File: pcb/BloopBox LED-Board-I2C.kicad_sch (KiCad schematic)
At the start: 14 parts, among them J1 I2C, J2 V_BM, U1 IS31FL3199

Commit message: fix: add part numbers
Add missing LSCS Part numbers
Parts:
- removed C2: 1u, Capacitor_SMD:C_0402_1005Metric, symbol Device:C_Small
- removed C3: 100n, Capacitor_SMD:C_0402_1005Metric, symbol Device:C_Small
- C1: LCSC (none) -> C52923
- C4, C5: LCSC (none) -> C1525
- R1: LCSC (none) -> C25741
- U1: footprint Package_DFN_QFN:QFN-20-1EP_3x3mm_P0.4mm_EP1.65x1.65mm -> Package_DFN_QFN:QFN-20-1EP_3x3mm_P0.4mm_EP1.65x1.65mm_ThermalVias
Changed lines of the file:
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@@
   (junction (at 45.72 127) (diameter 0) (color 0 0 0 0)
   )
-  (junction (at 104.14 73.66) (diameter 0) (color 0 0 0 0)
-  )
   (junction (at 71.12 127) (diameter 0) (color 0 0 0 0)
   )
   (junction (at 71.12 81.28) (diameter 0) (color 0 0 0 0)
-  )
-  (junction (at 96.52 73.66) (diameter 0) (color 0 0 0 0)
   )
   (junction (at 121.92 73.66) (diameter 0) (color 0 0 0 0)
@@
     (stroke (width 0) (type default) (color 0 0 0 0))
   )
-  (wire (pts (xy 71.12 73.66) (xy 96.52 73.66))
-    (stroke (width 0) (type default) (color 0 0 0 0))
-  )
   (wire (pts (xy 177.8 78.74) (xy 177.8 73.66))
     (stroke (width 0) (type default) (color 0 0 0 0))
@@
     (stroke (width 0) (type default) (color 0 0 0 0))
   )
-  (wire (pts (xy 104.14 81.28) (xy 104.14 83.82))
-    (stroke (width 0) (type default) (color 0 0 0 0))
-  )
   (wire (pts (xy 83.82 115.57) (xy 182.88 115.57))
     (stroke (width 0) (type default) (color 0 0 0 0))
@@
     (stroke (width 0) (type default) (color 0 0 0 0))
   )
-  (wire (pts (xy 96.52 73.66) (xy 96.52 76.2))
-    (stroke (width 0) (type default) (color 0 0 0 0))
-  )
   (wire (pts (xy 68.58 81.28) (xy 71.12 81.28))
     (stroke (width 0) (type default) (color 0 0 0 0))
@@
     (stroke (width 0) (type default) (color 0 0 0 0))
   )
-  (wire (pts (xy 104.14 73.66) (xy 121.92 73.66))
-    (stroke (width 0) (type default) (color 0 0 0 0))
-  )
   (wire (pts (xy 149.86 73.66) (xy 121.92 73.66))
     (stroke (width 0) (type default) (color 0 0 0 0))
@@
     (stroke (width 0) (type default) (color 0 0 0 0))
   )
-  (wire (pts (xy 96.52 81.28) (xy 96.52 83.82))
-    (stroke (width 0) (type default) (color 0 0 0 0))
-  )
   (wire (pts (xy 116.84 92.71) (xy 116.84 88.9))
     (stroke (width 0) (type default) (color 0 0 0 0))
@@
     (stroke (width 0) (type default) (color 0 0 0 0))
   )
-  (wire (pts (xy 96.52 73.66) (xy 104.14 73.66))
+  (wire (pts (xy 71.12 73.66) (xy 121.92 73.66))
     (stroke (width 0) (type default) (color 0 0 0 0))
   )
@@
   )
   (wire (pts (xy 53.34 110.49) (xy 53.34 127))
-    (stroke (width 0) (type default) (color 0 0 0 0))
-  )
-  (wire (pts (xy 104.14 73.66) (xy 104.14 76.2))
     (stroke (width 0) (type default) (color 0 0 0 0))
   )
@@
       (effects (font (size 1.27 1.27)) hide)
     )
+    (property "LCSC" "C25741" (id 4) (at 36.83 113.03 0)
+      (effects (font (size 1.27 1.27)) hide)
+    )
     (pin "1")
     (pin "2")
@@
     )
     (pin "1")
-  )
-  (symbol (lib_id "Device:C_Small") (at 96.52 78.74 180) (unit 1)
-    (in_bom yes) (on_board yes) (fields_autoplaced)
-    (property "Reference" "C2" (id 0) (at 98.8441 77.8989 0)
-      (effects (font (size 1.27 1.27)) (justify right))
-    )
-    (property "Value" "1u" (id 1) (at 98.8441 80.4358 0)
-      (effects (font (size 1.27 1.27)) (justify right))
-    )
-    (property "Footprint" "Capacitor_SMD:C_0402_1005Metric" (id 2) (at 96.52 78.74 0)
-      (effects (font (size 1.27 1.27)) hide)
-    )
-    (property "Datasheet" "~" (id 3) (at 96.52 78.74 0)
-      (effects (font (size 1.27 1.27)) hide)
-    )
-    (pin "1")
-    (pin "2")
   )
   (symbol (lib_id "power:GND") (at 60.96 81.28 270) (unit 1)
@@
       (effects (font (size 1.27 1.27)) (justify left))
     )
-    (property "Footprint" "Package_DFN_QFN:QFN-20-1EP_3x3mm_P0.4mm_EP1.65x1.65mm" (id 2) (at 71.12 82.55 0)
+    (property "Footprint" "Package_DFN_QFN:QFN-20-1EP_3x3mm_P0.4mm_EP1.65x1.65mm_ThermalVias" (id 2) (at 71.12 82.55 0)
       (effects (font (size 1.27 1.27)) hide)
     )
@@
     (pin "9")
   )
-  (symbol (lib_id "power:GND") (at 104.14 83.82 0) (unit 1)
-    (in_bom yes) (on_board yes) (fields_autoplaced)
-    (property "Reference" "#PWR07" (id 0) (at 104.14 90.17 0)
-      (effects (font (size 1.27 1.27)) hide)
-    )
-    (property "Value" "GND" (id 1) (at 106.045 85.5238 0)
-      (effects (font (size 1.27 1.27)) (justify left))
-    )
-    (property "Footprint" "" (id 2) (at 104.14 83.82 0)
-      (effects (font (size 1.27 1.27)) hide)
-    )
-    (property "Datasheet" "" (id 3) (at 104.14 83.82 0)
-      (effects (font (size 1.27 1.27)) hide)
-    )
-    (pin "1")
-  )
   (symbol (lib_id "Connector_Generic:Conn_01x01") (at 30.48 53.34 180) (unit 1)
     (in_bom yes) (on_board yes) (fields_autoplaced)
@@
       (effects (font (size 1.27 1.27)) hide)
     )
+    (property "LCSC" "C52923" (id 4) (at 66.04 73.66 0)
+      (effects (font (size 1.27 1.27)) hide)
+    )
     (pin "1")
     (pin "2")
@@
       (effects (font (size 1.27 1.27)) hide)
     )
-    (pin "1")
-    (pin "2")
-  )
-  (symbol (lib_id "power:GND") (at 96.52 83.82 0) (unit 1)
-    (in_bom yes) (on_board yes) (fields_autoplaced)
-    (property "Reference" "#PWR06" (id 0) (at 96.52 90.17 0)
-      (effects (font (size 1.27 1.27)) hide)
-    )
-    (property "Value" "GND" (id 1) (at 98.425 85.5238 0)
-      (effects (font (size 1.27 1.27)) (justify left))
-    )
-    (property "Footprint" "" (id 2) (at 96.52 83.82 0)
-      (effects (font (size 1.27 1.27)) hide)
-    )
-    (property "Datasheet" "" (id 3) (at 96.52 83.82 0)
-      (effects (font (size 1.27 1.27)) hide)
-    )
-    (pin "1")
+    (property "LCSC" "C1525" (id 4) (at 66.04 81.28 0)
+      (effects (font (size 1.27 1.27)) hide)
+    )
+    (pin "1")
+    (pin "2")
   )
   (symbol (lib_id "Device:C_Small") (at 45.72 113.03 180) (unit 1)
@@
       (effects (font (size 1.27 1.27)) hide)
     )
-    (pin "1")
-    (pin "2")
-  )
-  (symbol (lib_id "Device:C_Small") (at 104.14 78.74 180) (unit 1)
-    (in_bom yes) (on_board yes) (fields_autoplaced)
-    (property "Reference" "C3" (id 0) (at 106.4641 77.8989 0)
-      (effects (font (size 1.27 1.27)) (justify right))
-    )
-    (property "Value" "100n" (id 1) (at 106.4641 80.4358 0)
-      (effects (font (size 1.27 1.27)) (justify right))
-    )
-    (property "Footprint" "Capacitor_SMD:C_0402_1005Metric" (id 2) (at 104.14 78.74 0)
-      (effects (font (size 1.27 1.27)) hide)
-    )
-    (property "Datasheet" "~" (id 3) (at 104.14 78.74 0)
+    (property "LCSC" "C1525" (id 4) (at 45.72 113.03 0)
       (effects (font (size 1.27 1.27)) hide)
     )
@@
       (reference "#PWR05") (unit 1) (value "GND") (footprint "")
     )
-    (path "/dbcecde5-1d68-41ea-8940-39f26b5eec6b"
-      (reference "#PWR06") (unit 1) (value "GND") (footprint "")
-    )
-    (path "/56eb8215-4817-443a-ae37-57edd7e00e9a"
-      (reference "#PWR07") (unit 1) (value "GND") (footprint "")
-    )
     (path "/0ad71f82-5b4f-4881-8640-a72fd7d96db2"
       (reference "#PWR08") (unit 1) (value "VCC") (footprint "")
@@
       (reference "C1") (unit 1) (value "1u") (footprint "Capacitor_SMD:C_0402_1005Metric")
     )
-    (path "/200cf5e6-e58a-40f9-b45f-b55c95de0d8b"
-      (reference "C2") (unit 1) (value "1u") (footprint "Capacitor_SMD:C_0402_1005Metric")
-    )
-    (path "/e057b853-9a40-4a3e-8bf4-4b4fa06f5df1"
-      (reference "C3") (unit 1) (value "100n") (footprint "Capacitor_SMD:C_0402_1005Metric")
-    )
     (path "/cdfd3c02-6223-4acd-8411-8f5e2a574677"
       (reference "C4") (unit 1) (value "100n") (footprint "Capacitor_SMD:C_0402_1005Metric")
@@
     )
     (path "/4e91f506-e77b-4b90-ab1f-968dcca557ce"
-      (reference "U1") (unit 1) (value "IS31FL3199") (footprint "Package_DFN_QFN:QFN-20-1EP_3x3mm_P0.4mm_EP1.65x1.65mm")
-    )
-  )
+      (reference "U1") (unit 1) (value "IS31FL3199") (footprint "Package_DFN_QFN:QFN-20-1EP_3x3mm_P0.4mm_EP1.65x1.65mm_ThermalVias")
+    )
+  )

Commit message: fix: add power flags
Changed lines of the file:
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@@
     (pin "4")
+  )
+  (symbol (lib_id "power:PWR_FLAG") (at -58.42 177.8 0) (unit 1)
+    (in_bom yes) (on_board yes) (fields_autoplaced)
+    (property "Reference" "#FLG0102" (id 0) (at -58.42 175.895 0)
+      (effects (font (size 1.27 1.27)) hide)
+    )
+    (property "Value" "PWR_FLAG" (id 1) (at -58.42 174.2242 0))
+    (property "Footprint" "" (id 2) (at -58.42 177.8 0)
+      (effects (font (size 1.27 1.27)) hide)
+    )
+    (property "Datasheet" "~" (id 3) (at -58.42 177.8 0)
+      (effects (font (size 1.27 1.27)) hide)
+    )
+    (pin "1")
   )
   (symbol (lib_id "power:GND") (at 71.12 129.54 0) (unit 1)
@@
     (pin "1")
   )
+  (symbol (lib_id "power:PWR_FLAG") (at -48.26 177.8 0) (unit 1)
+    (in_bom yes) (on_board yes) (fields_autoplaced)
+    (property "Reference" "#FLG0101" (id 0) (at -48.26 175.895 0)
+      (effects (font (size 1.27 1.27)) hide)
+    )
+    (property "Value" "PWR_FLAG" (id 1) (at -48.26 174.2242 0))
+    (property "Footprint" "" (id 2) (at -48.26 177.8 0)
+      (effects (font (size 1.27 1.27)) hide)
+    )
+    (property "Datasheet" "~" (id 3) (at -48.26 177.8 0)
+      (effects (font (size 1.27 1.27)) hide)
+    )
+    (pin "1")
+  )
   (symbol (lib_id "Mechanical:MountingHole") (at 172.72 144.78 0) (unit 1)
     (in_bom yes) (on_board yes) (fields_autoplaced)
@@
     )
     (property "Datasheet" "" (id 3) (at 71.12 71.12 0)
+      (effects (font (size 1.27 1.27)) hide)
+    )
+    (pin "1")
+  )
+  (symbol (lib_id "power:VCC") (at -58.42 177.8 180) (unit 1)
+    (in_bom yes) (on_board yes) (fields_autoplaced)
+    (property "Reference" "#PWR0102" (id 0) (at -58.42 173.99 0)
+      (effects (font (size 1.27 1.27)) hide)
+    )
+    (property "Value" "VCC" (id 1) (at -57.023 179.5038 0)
+      (effects (font (size 1.27 1.27)) (justify right))
+    )
+    (property "Footprint" "" (id 2) (at -58.42 177.8 0)
+      (effects (font (size 1.27 1.27)) hide)
+    )
+    (property "Datasheet" "" (id 3) (at -58.42 177.8 0)
       (effects (font (size 1.27 1.27)) hide)
     )
@@
     (pin "4")
   )
+  (symbol (lib_id "power:GND") (at -48.26 177.8 0) (unit 1)
+    (in_bom yes) (on_board yes) (fields_autoplaced)
+    (property "Reference" "#PWR0101" (id 0) (at -48.26 184.15 0)
+      (effects (font (size 1.27 1.27)) hide)
+    )
+    (property "Value" "GND" (id 1) (at -46.355 179.5038 0)
+      (effects (font (size 1.27 1.27)) (justify left))
+    )
+    (property "Footprint" "" (id 2) (at -48.26 177.8 0)
+      (effects (font (size 1.27 1.27)) hide)
+    )
+    (property "Datasheet" "" (id 3) (at -48.26 177.8 0)
+      (effects (font (size 1.27 1.27)) hide)
+    )
+    (pin "1")
+  )
   (symbol (lib_id "Mechanical:MountingHole") (at 172.72 149.86 0) (unit 1)
     (in_bom yes) (on_board yes) (fields_autoplaced)
@@
   )
   (symbol_instances
+    (path "/7ffca218-bf34-42a3-b54e-1156e20a2407"
+      (reference "#FLG0101") (unit 1) (value "PWR_FLAG") (footprint "")
+    )
+    (path "/2f3794e2-0388-474a-a5f8-8719700774e0"
+      (reference "#FLG0102") (unit 1) (value "PWR_FLAG") (footprint "")
+    )
     (path "/f62ee4b1-41a8-482d-8766-c90c24d9764e"
       (reference "#PWR01") (unit 1) (value "GND") (footprint "")
@@
       (reference "#PWR09") (unit 1) (value "GND") (footprint "")
     )
+    (path "/eed4aed9-a5f0-44a1-806d-93e8250a5d0c"
+      (reference "#PWR0101") (unit 1) (value "GND") (footprint "")
+    )
+    (path "/9dd6ba33-7dfd-4f6b-bdcd-a0e6fd7103b0"
+      (reference "#PWR0102") (unit 1) (value "VCC") (footprint "")
+    )
     (path "/9f65a06b-bab6-4f77-ba97-01c96678c3dc"

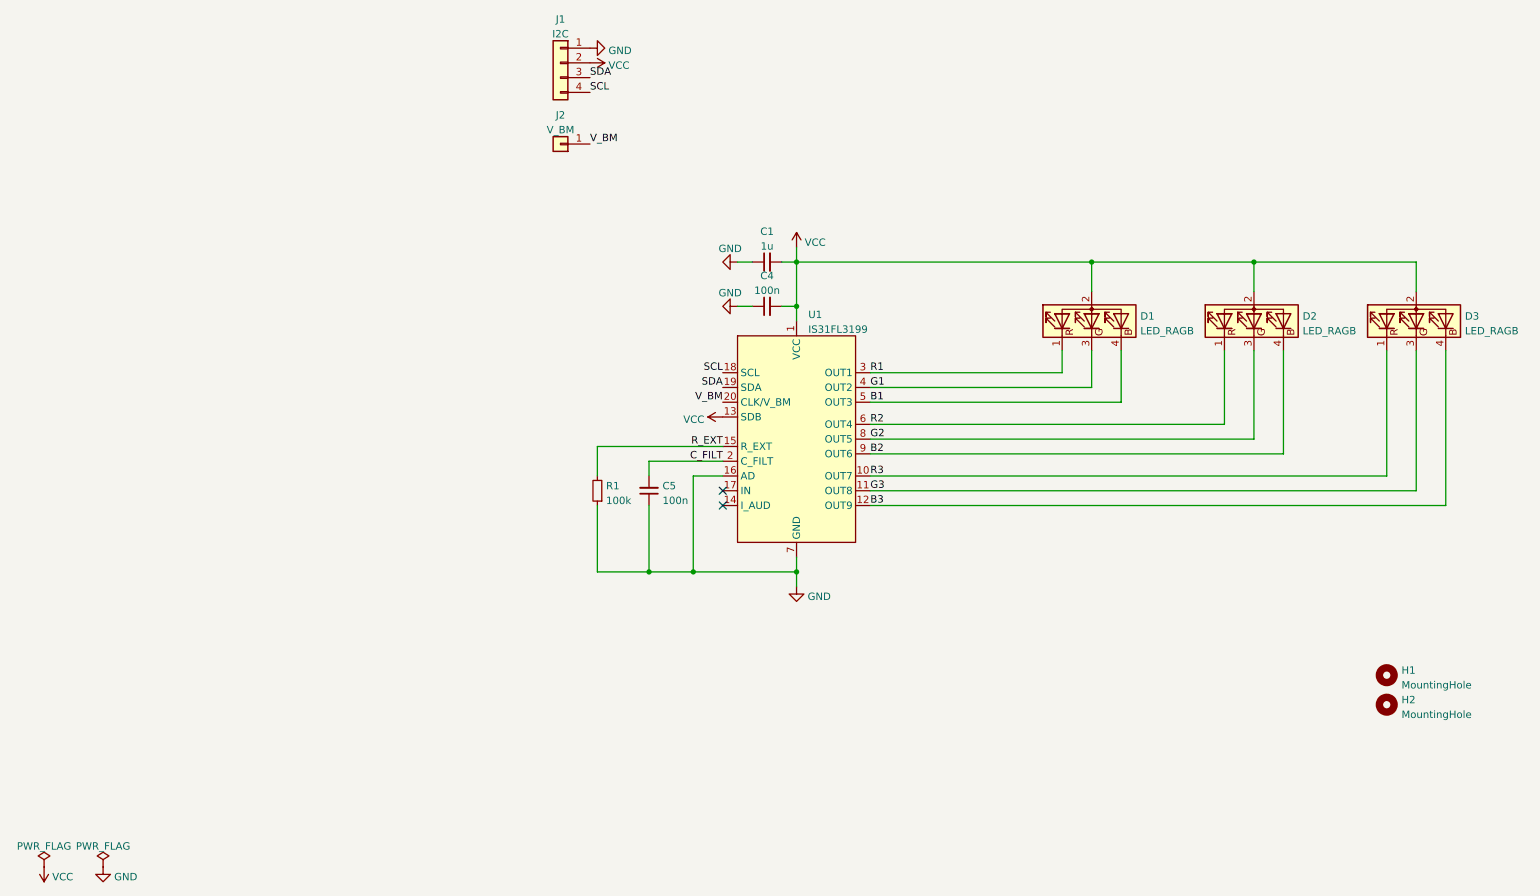
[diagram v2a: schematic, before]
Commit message: feat: change LED controller to AW2013
replace the IS31FL3199 with AW2013 and remove additional LED footprints
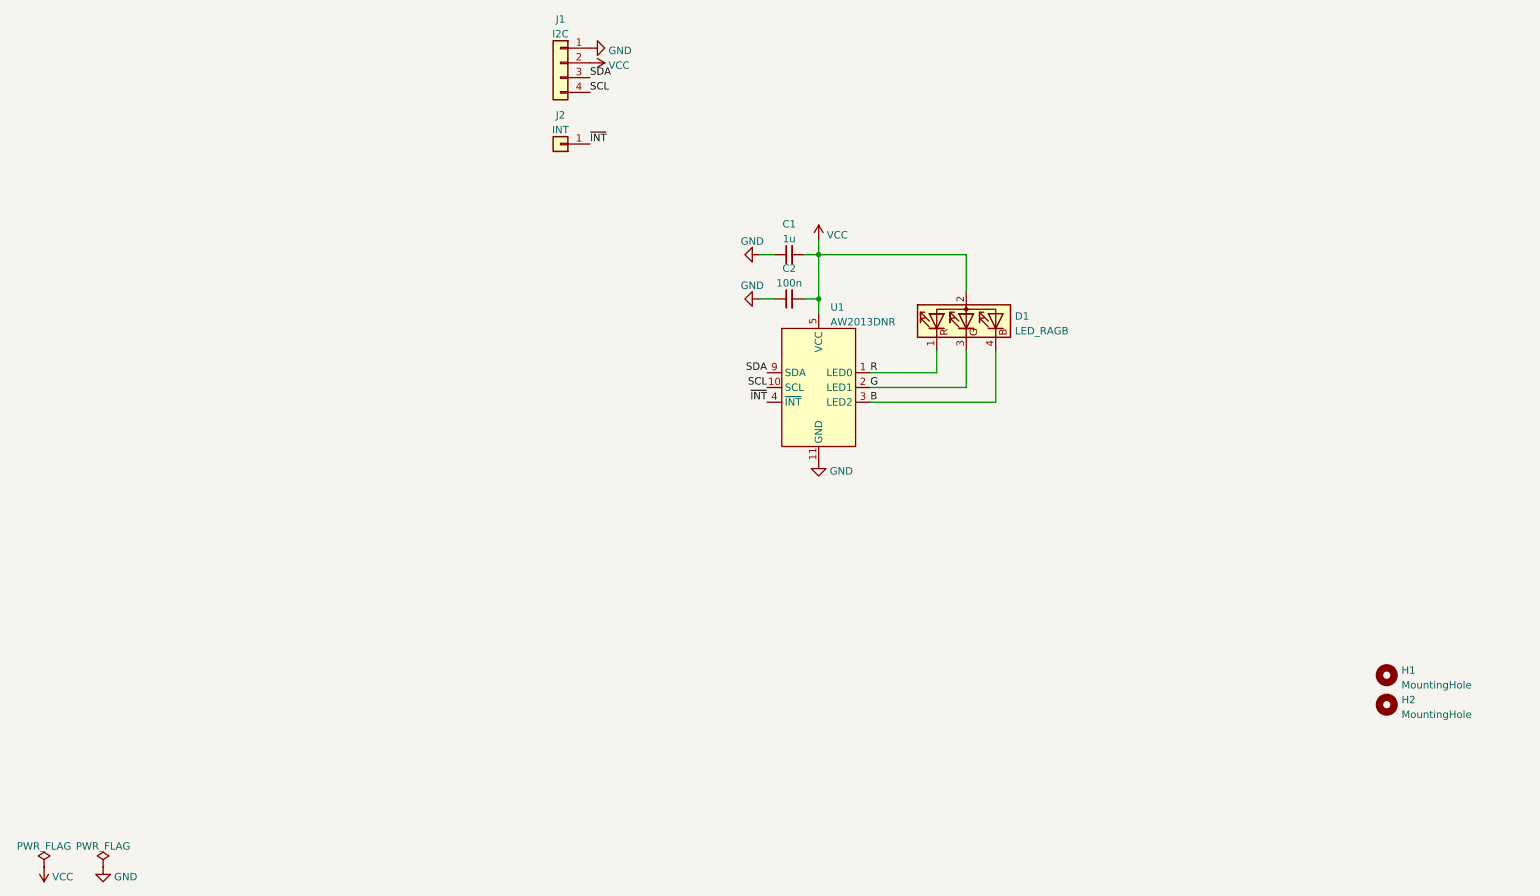
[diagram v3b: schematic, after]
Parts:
- removed C5: 100n, Capacitor_SMD:C_0402_1005Metric, symbol Device:C_Small
- removed D2, D3: LED_RAGB, LED_THT:LED_D5.0mm-4_RGB_Staggered_Pins, symbol Device:LED_RAGB
- removed R1: 100k, Resistor_SMD:R_0402_1005Metric, symbol Device:R_Small
- removed U1: IS31FL3199, Package_DFN_QFN:QFN-20-1EP_3x3mm_P0.4mm_EP1.65x1.65mm_ThermalVias, symbol My_Symbols:IS31FL3199
- added U1: AW2013DNR, My_Footprints:DFN-10-1EP_2x2mm_P0.4mm_EP0.8x1.4, symbol My_Symbols:AW2013DNR
- J2: value V_BM -> INT
- renumbered C4 to C2
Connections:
- net GND: now also U1.11 (GND)
- net SCL: now also U1.10 (SCL)
- net SDA: now also U1.9 (SDA)
- net VCC: now also U1.5 (VCC)
- net B1 renamed B
- net B: now also U1.3 (LED2)
- net G1 renamed G
- net G: now also U1.2 (LED1)
- net R1 renamed R
- net R: now also U1.1 (LED0)
- net V_BM renamed ~{INT}
- net ~{INT}: now also U1.4 (~{INT})
- no-connect marks 2 -> 0
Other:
- moved on the sheet: C1, C2, D1

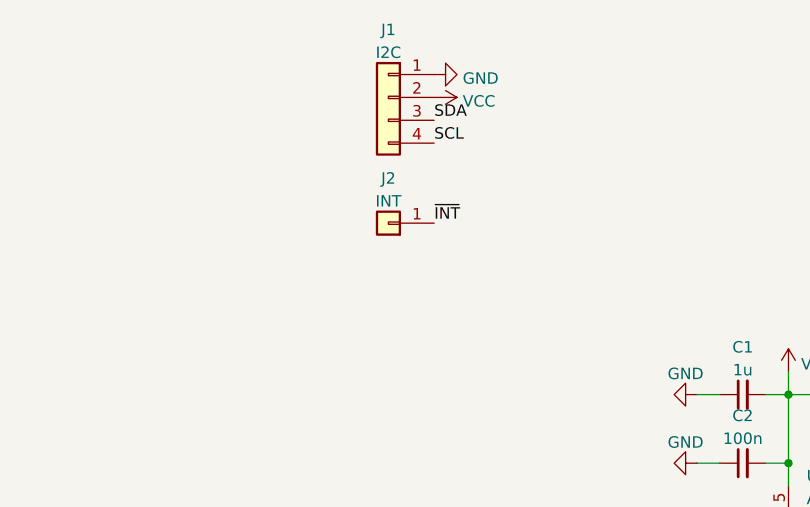
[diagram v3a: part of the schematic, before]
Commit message: feat: flip sides of LED and connector
Flip the LED to the bottom and the connector to the top to make it possible to have the connector assembled at the factory

Also updating sources to KiCad 8
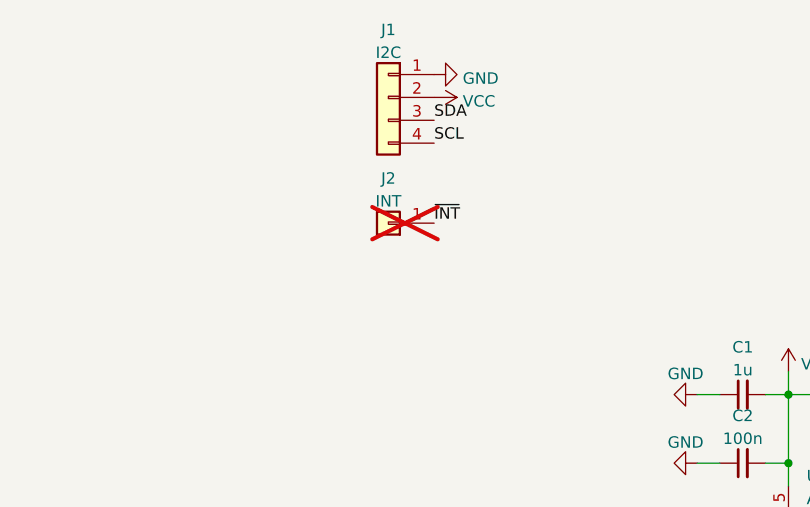
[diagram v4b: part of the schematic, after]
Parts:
- H1, H2: now left out of the parts list
- J1: LCSC (none) -> C49994
- J2: now not fitted
